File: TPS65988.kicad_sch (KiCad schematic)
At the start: 11 parts, among them J2 USB_C_Receptacle, J3 USB_C_Receptacle, J4 Conn_01x04, U11 TPS65988

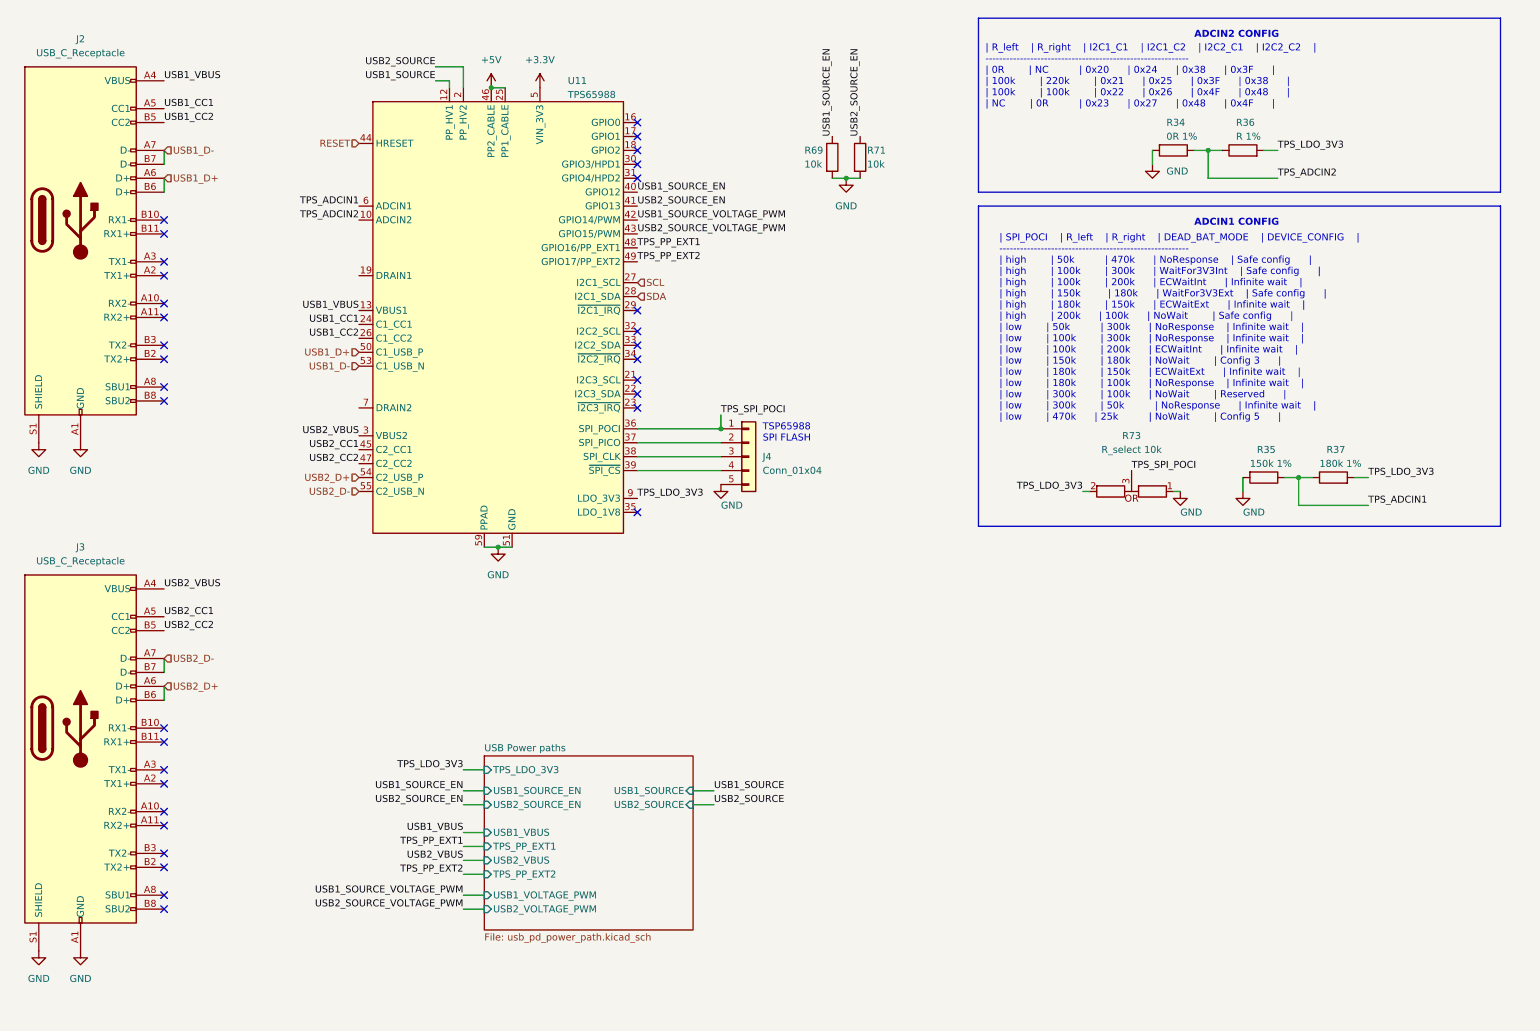
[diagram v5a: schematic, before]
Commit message: minor optimized pinassignement, added capacitors, added connectors
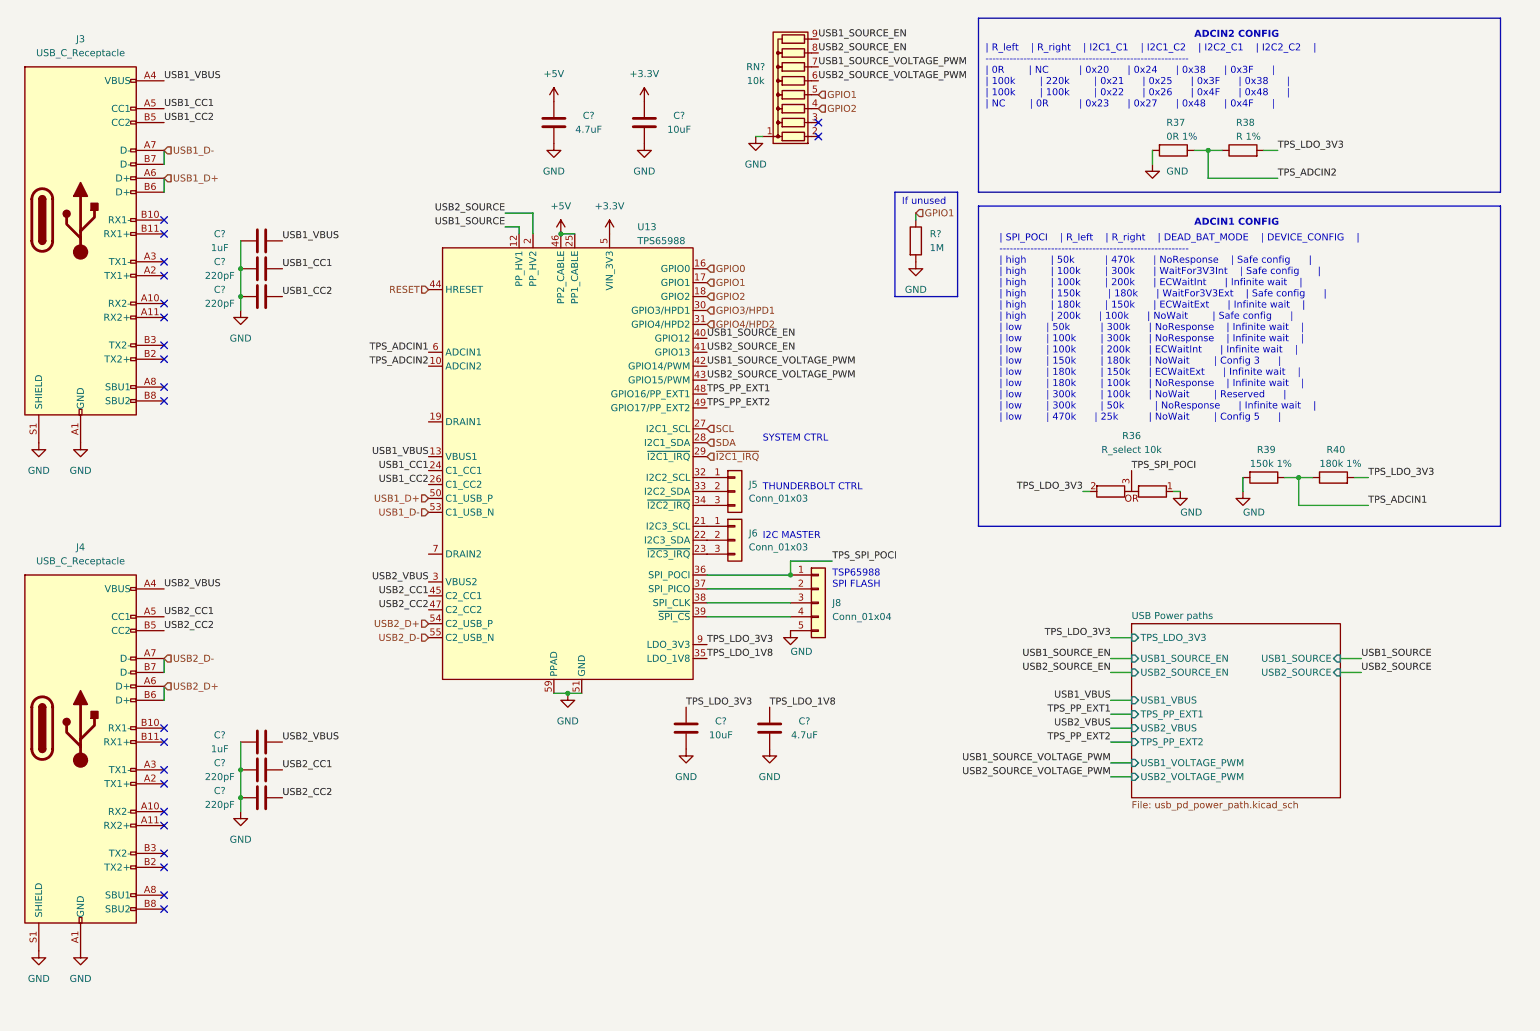
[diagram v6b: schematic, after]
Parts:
- removed R69, R71: 10k, symbol Device:R
- added C? (x4): 220pF, symbol Device:C
- added C? (x2): 4.7uF, symbol Device:C
- added C? (x2): 1uF, symbol Device:C
- added C? (x2): 10uF, symbol Device:C
- added J5, J6: Conn_01x03, symbol Connector_Generic:Conn_01x03
- added R?: 1M, symbol Device:R
- added RN?: 10k, Resistor_THT:R_Array_SIP9, symbol Device:R_Network08
- renumbered J2 to J3, J3 to J4, J4 to J8, R73 to R36, R34 to R37, R36 to R38, R35 to R39, R37 to R40, U11 to U13
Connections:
- net +3.3V: now also C?.2
- net +5V: now also C?.2
- net GND: now also C?.1, C?.1, C?.1, C?.1, C?.2, C?.2, C?.2, C?.2, C?.2, C?.2, R?.2, RN?.1 (common)
- net TPS_LDO_3V3: now also C?.2
- net USB1_CC1: now also C?.1
- net USB1_CC2: now also C?.1
- net USB1_SOURCE_EN: now also RN?.9 (R8)
- net USB1_SOURCE_VOLTAGE_PWM: now also RN?.7 (R6)
- net USB1_VBUS: now also C?.1
- net USB2_CC1: now also C?.1
- net USB2_CC2: now also C?.1
- net USB2_SOURCE_EN: now also RN?.8 (R7)
- net USB2_SOURCE_VOLTAGE_PWM: now also RN?.6 (R5)
- net USB2_VBUS: now also C?.1
- net GPIO0: now reaches U13.16 (GPIO0)
- net GPIO1: now reaches U13.17 (GPIO1)
- net GPIO1: now also R?.1, RN?.5 (R4)
- net GPIO2: now reaches U13.18 (GPIO2)
- net GPIO2: now also RN?.4 (R3)
- net at U13.21 (I2C3_SCL): now also J6.1 (Pin_1)
- net at U13.22 (I2C3_SDA): now also J6.2 (Pin_2)
- net at U13.23 (~{I2C3_IRQ}): now also J6.3 (Pin_3)
- net ~{I2C1_IRQ}: now reaches U13.29 (~{I2C1_IRQ})
- net GPIO3/HPD1: now reaches U13.30 (GPIO3/HPD1)
- net GPIO4/HPD2: now reaches U13.31 (GPIO4/HPD2)
- net at U13.32 (I2C2_SCL): now also J5.1 (Pin_1)
- net at U13.33 (I2C2_SDA): now also J5.2 (Pin_2)
- net at U13.34 (~{I2C2_IRQ}): now also J5.3 (Pin_3)
- net TPS_LDO_1V8: now reaches U13.35 (LDO_1V8)
- net TPS_LDO_1V8: now also C?.2
- no-connect marks 33 -> 22
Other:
- note added: "I2C MASTER"
- note added: "If unused"
- note added: "SYSTEM CTRL"
- note added: "THUNDERBOLT CTRL"
- moved on the sheet: J8, U13

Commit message: PI LC lowpass filter, added CP2012 reset, added connectors
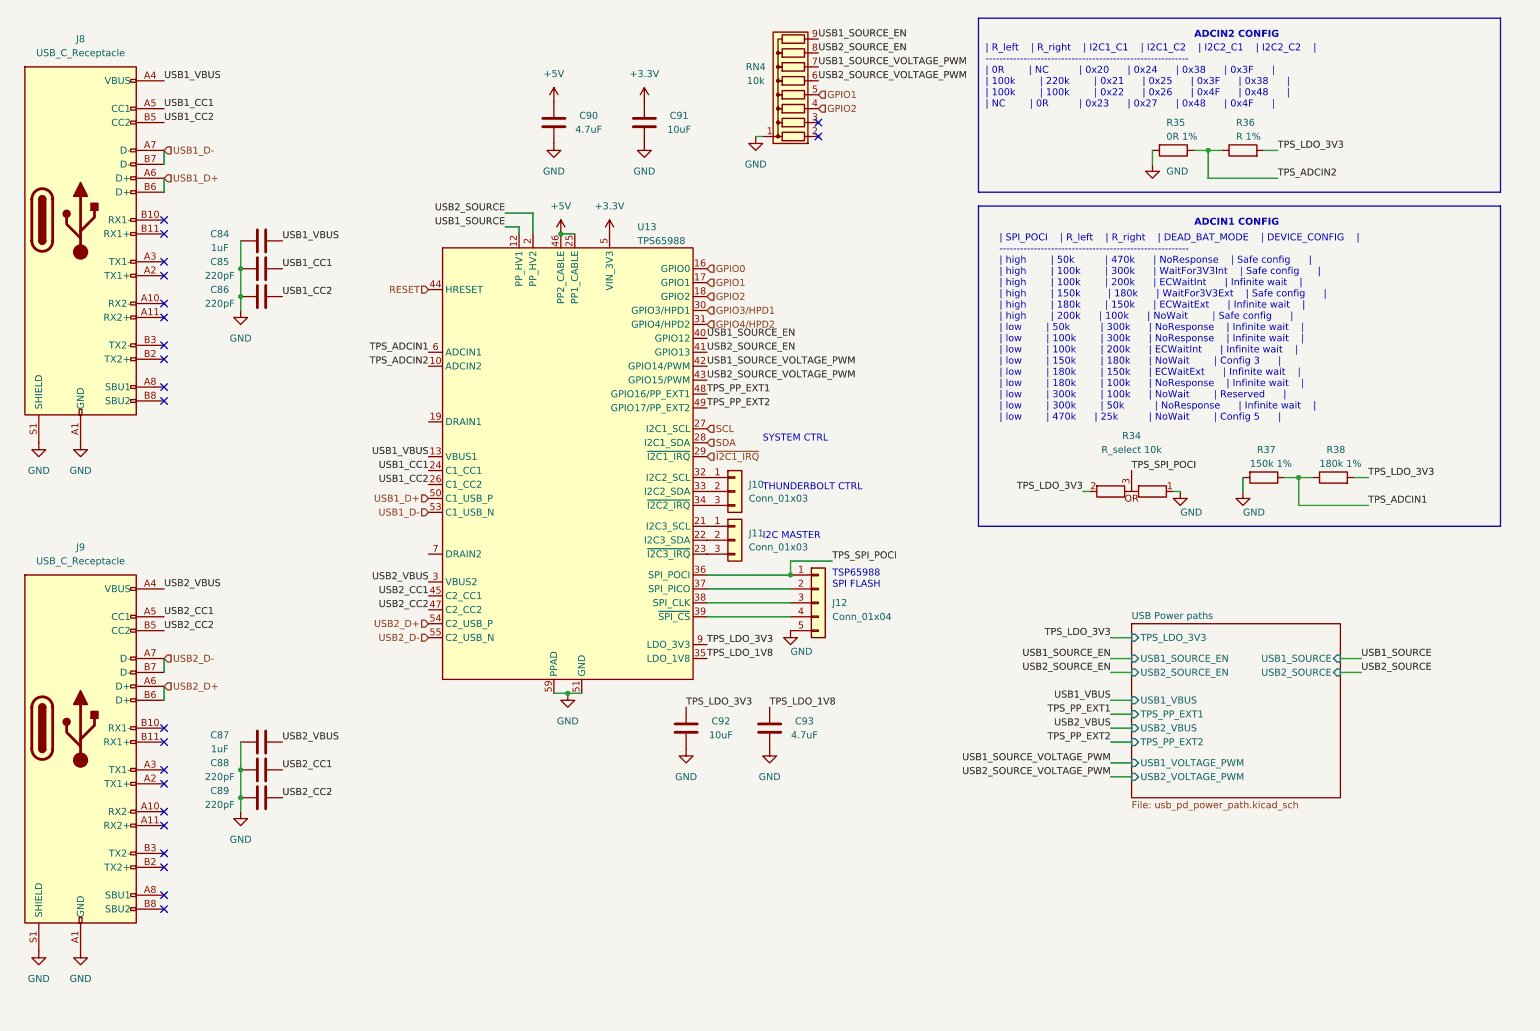
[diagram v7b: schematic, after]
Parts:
- removed R?: 1M, symbol Device:R
- gave numbers to parts that had none: 11
- renumbered J5 to J10, J6 to J11, J8 to J12, J3 to J8, J4 to J9, R36 to R34, R37 to R35, R38 to R36, R39 to R37, R40 to R38
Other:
- note removed: "If unused"

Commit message: datasheet checkout, added couple of capacitors for usb-c, groupd some scheatics
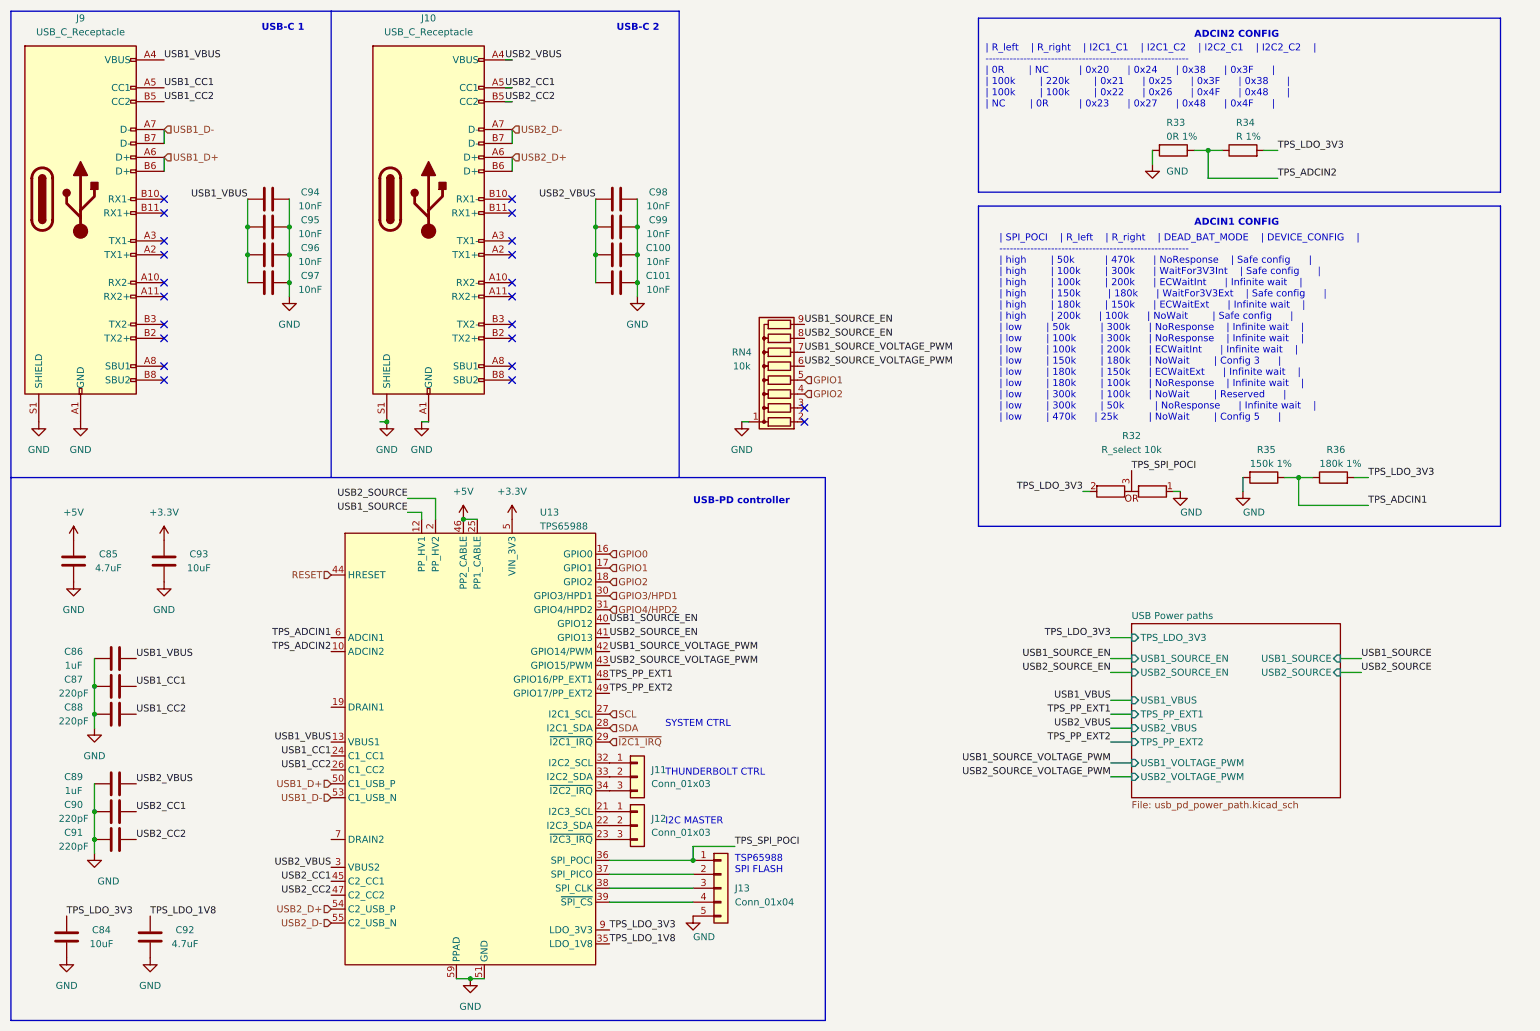
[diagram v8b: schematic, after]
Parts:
- added C100, C101, C94, C95, C96, C97, C98, C99: 10nF, symbol Device:C
- renumbered C92 to C84, C90 to C85, C84 to C86, C85 to C87, C86 to C88, C87 to C89, C88 to C90, C89 to C91, C93 to C92, C91 to C93, J9 to J10, J10 to J11, J11 to J12, J12 to J13, J8 to J9, R34 to R32, R35 to R33, R36 to R34, R37 to R35, R38 to R36
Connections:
- net GND: now also C100.2, C101.2, C94.2, C95.2, C96.2, C97.2, C98.2, C99.2
- net USB1_VBUS: now also C94.1, C95.1, C96.1, C97.1
- net USB2_VBUS: now also C100.1, C101.1, C98.1, C99.1
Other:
- note added: "USB-C 1"
- note added: "USB-C 2"
- note added: "USB-PD controller"
- moved on the sheet: C84, C85, C86, C87, C88, C89, C90, C91, C92, C93, J10, J11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
